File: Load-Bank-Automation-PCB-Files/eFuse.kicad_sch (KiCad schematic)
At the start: 14 parts, among them Q3 NMOS, U7 LM5069MM-1

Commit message: Nothing new
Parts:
- R13: value R -> 6.5m
- R18: value 100k -> R_{PGD}
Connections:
- net V_{DD} is gone; now on net V+_{in}: R18.2
- net PGOOD: no longer names the net of R18.1, U7.8 (PGD)
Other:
- note added: "Calculations: * Current Limit: Is when 48.5mv<=V_{CL}<=61.5mv -> 48.5mV/7.5A=R_{13}=${/c82c4769-33eb-46b7-8d07-39045014a3da/eb9b9647-818b-4f6a-aec9-7481a1a3b43c/4e0619fb-b7ea-493d-b159-72357478fd6a/6879bab9-d947-4c13-8fcf-4238d3b2053c:value}ohm * R_{PWR} is used to determine the thermal limit of Q1 MOSFET, the chip uses the current from R_{sense} and the voltage from SENSE and OUT pins to find th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"
- moved on the sheet: C32, C33, C34, D2, D4, Q3, R13, R14, R15, R16, R17, R18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

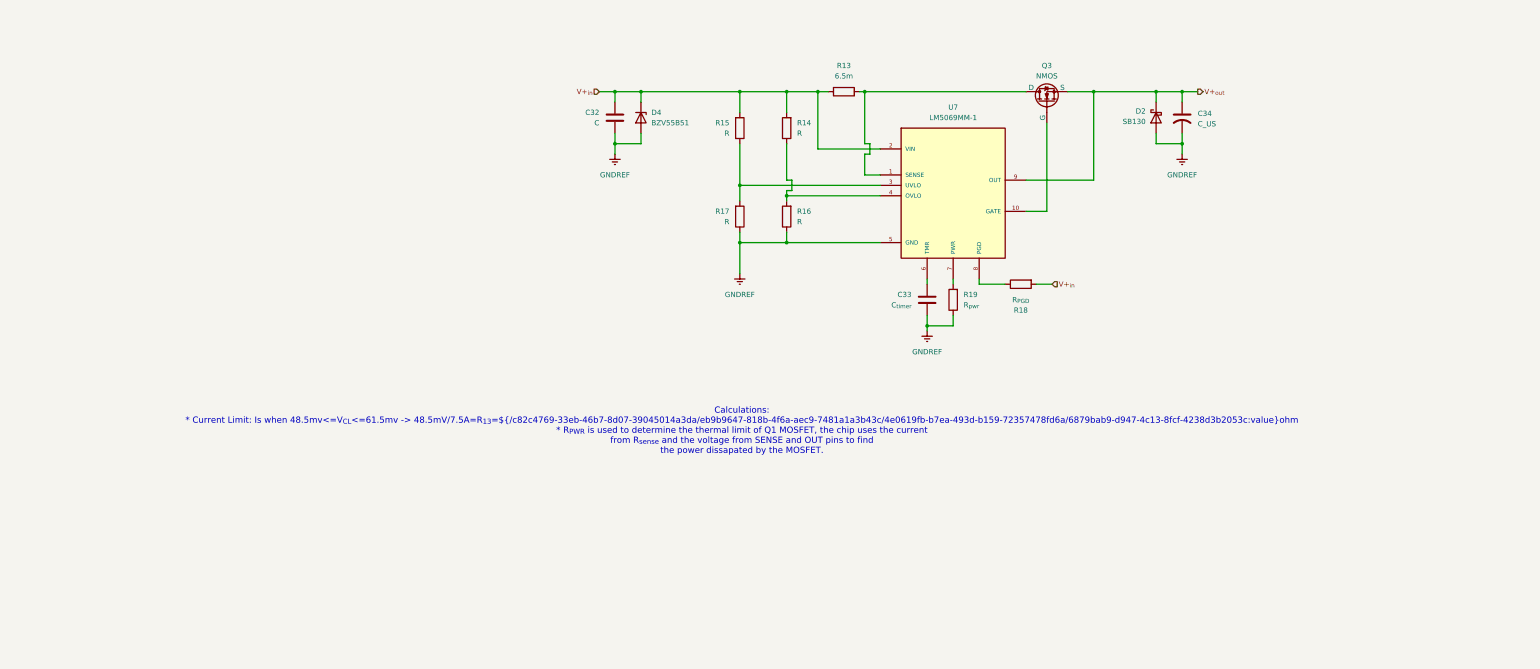
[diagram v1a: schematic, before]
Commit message: Completed eFuse and Starting on Layout
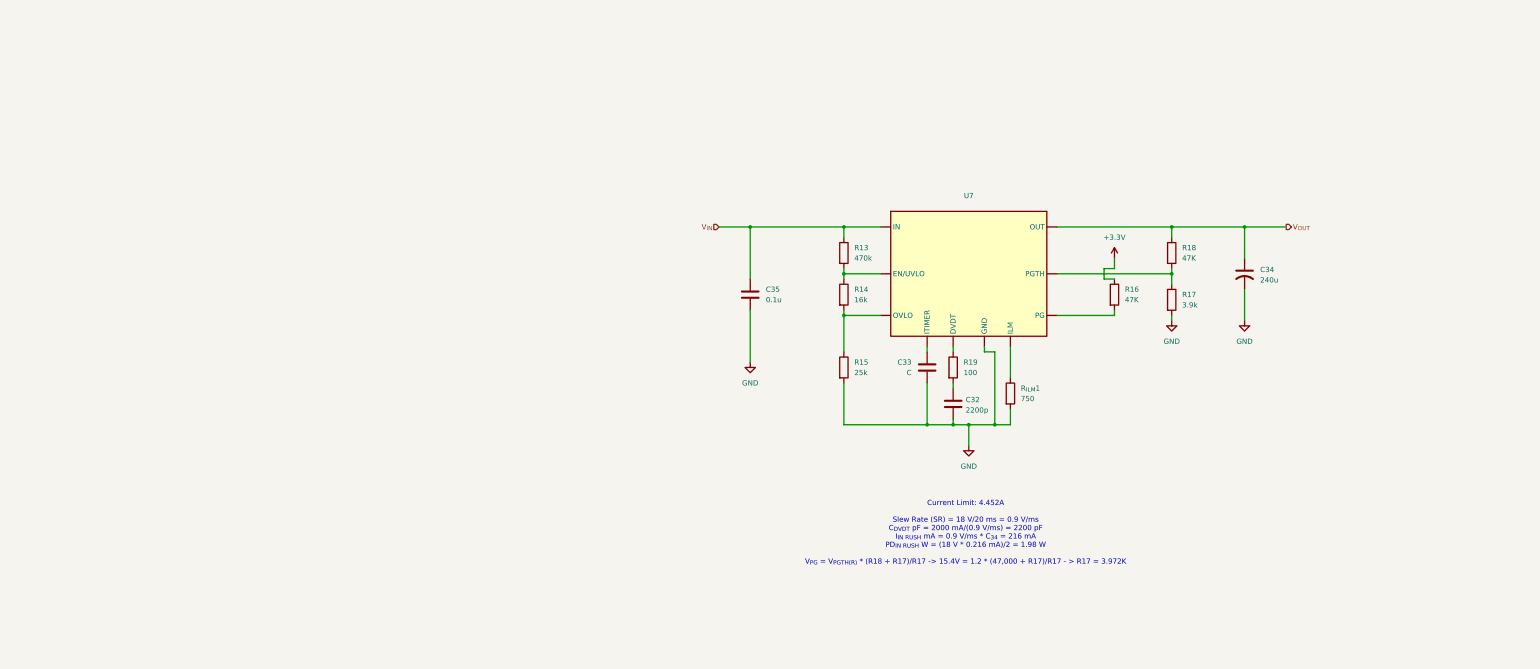
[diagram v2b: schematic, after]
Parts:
- removed D2: SB130, Diode_THT:D_DO-41_SOD81_P10.16mm_Horizontal, symbol Diode:SB130
- removed D4: BZV55B51, Diode_SMD:D_MiniMELF, symbol Diode:BZV55B51
- removed Q3: NMOS, symbol Simulation_SPICE:NMOS
- removed U7: LM5069MM-1, LM5069MM-1:SOP50P490X110-10N, symbol LM5069MM-1:LM5069MM-1
- added C35: 0.1u, Resistor_SMD:R_0603_1608Metric, symbol Device:C
- added R_{ILM}1: 750, Resistor_SMD:R_0603_1608Metric, symbol Device:R
- added U7: ~, symbol Power_Protection:TPS259474LRPWR
- C32: value C -> 2200p; footprint (none) -> Resistor_SMD:R_0603_1608Metric
- C33: value C_{timer} -> C; footprint (none) -> Resistor_SMD:R_0603_1608Metric
- C34: value C_US -> 240u; footprint (none) -> Resistor_SMD:R_0603_1608Metric
- R13: value 6.5m -> 470k; footprint (none) -> Resistor_SMD:R_0603_1608Metric
- R14: value R -> 16k; footprint (none) -> Resistor_SMD:R_0603_1608Metric
- R15: value R -> 25k; footprint (none) -> Resistor_SMD:R_0603_1608Metric
- R16: value R -> 47K; footprint (none) -> Resistor_SMD:R_0603_1608Metric
- R17: value R -> 3.9k; footprint (none) -> Resistor_SMD:R_0603_1608Metric
- R18: value R_{PGD} -> 47K; footprint (none) -> Resistor_SMD:R_0603_1608Metric
- R19: value R_{pwr} -> 100; footprint (none) -> Resistor_SMD:R_0603_1608Metric
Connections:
- net V+_{out} is gone; now on net V_{OUT}: C34.1
- net GND: now reaches C33.1
- net GND: now also C32.2, C34.2, R15.2, R17.2, C35.2, R_{ILM}1.2, U7. (PG)
- net at R16.2: now also U7. (PG); no longer R14.1
- net at R15.1: now also R14.2, U7. (PG); no longer R17.2
- net V_{IN}: now reaches R13.1
- net V_{IN}: now also C35.1, U7. (PG)
- net at R19.2: now also C32.1
- net V_{OUT}: now reaches R18.1
- net V_{OUT}: now also U7. (PG)
- removed net GNDREF: C32.2, C33.2, C34.2, R16.1, R17.1, R19.1
- removed net V+_{in}: C32.1, R13.2, R14.2, R15.2, R18.2
- new net: R19.1, U7. (PG)
- new net: R_{ILM}1.1, U7. (PG)
- new net: R13.2, R14.1, U7. (PG)
- new net: R17.1, R18.2, U7. (PG)
- new net: C33.2, U7. (PG)
- new net +3.3V: R16.1
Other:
- note added: "Current Limit: 4.452A Slew Rate (SR) = 18 V/20 ms = 0.9 V/ms C_{DVDT} pF = 2000 mA/(0.9 V/ms) = 2200 pF I_{IN RUSH} mA = 0.9 V/ms * C_{34} = 216 mA PD_{IN RUSH} W = (18 V * 0.216 mA)/2 = 1.98 W V_{PG} = V_{PGTH(R)} * (R18 + R17)/R17 -> 15.4V = 1.2 * (47,000 + R17)/R17 - > R17 = 3.972K"
- note removed: "Calculations: * Current Limit: Is when 48.5mv<=V_{CL}<=61.5mv -> 48.5mV/7.5A=R_{13}=${/c82c4769-33eb-46b7-8d07-39045014a3da/eb9b9647-818b-4f6a-aec9-7481a1a3b43c/4e0619fb-b7ea-493d-b159-72357478fd6a/6879bab9-d947-4c13-8fcf-4238d3b2053c:value}ohm * R_{PWR} is used to determine the thermal limit of Q1 MOSFET, the chip uses the current from R_{sense} and the voltage from SENSE and OUT pins to find th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"

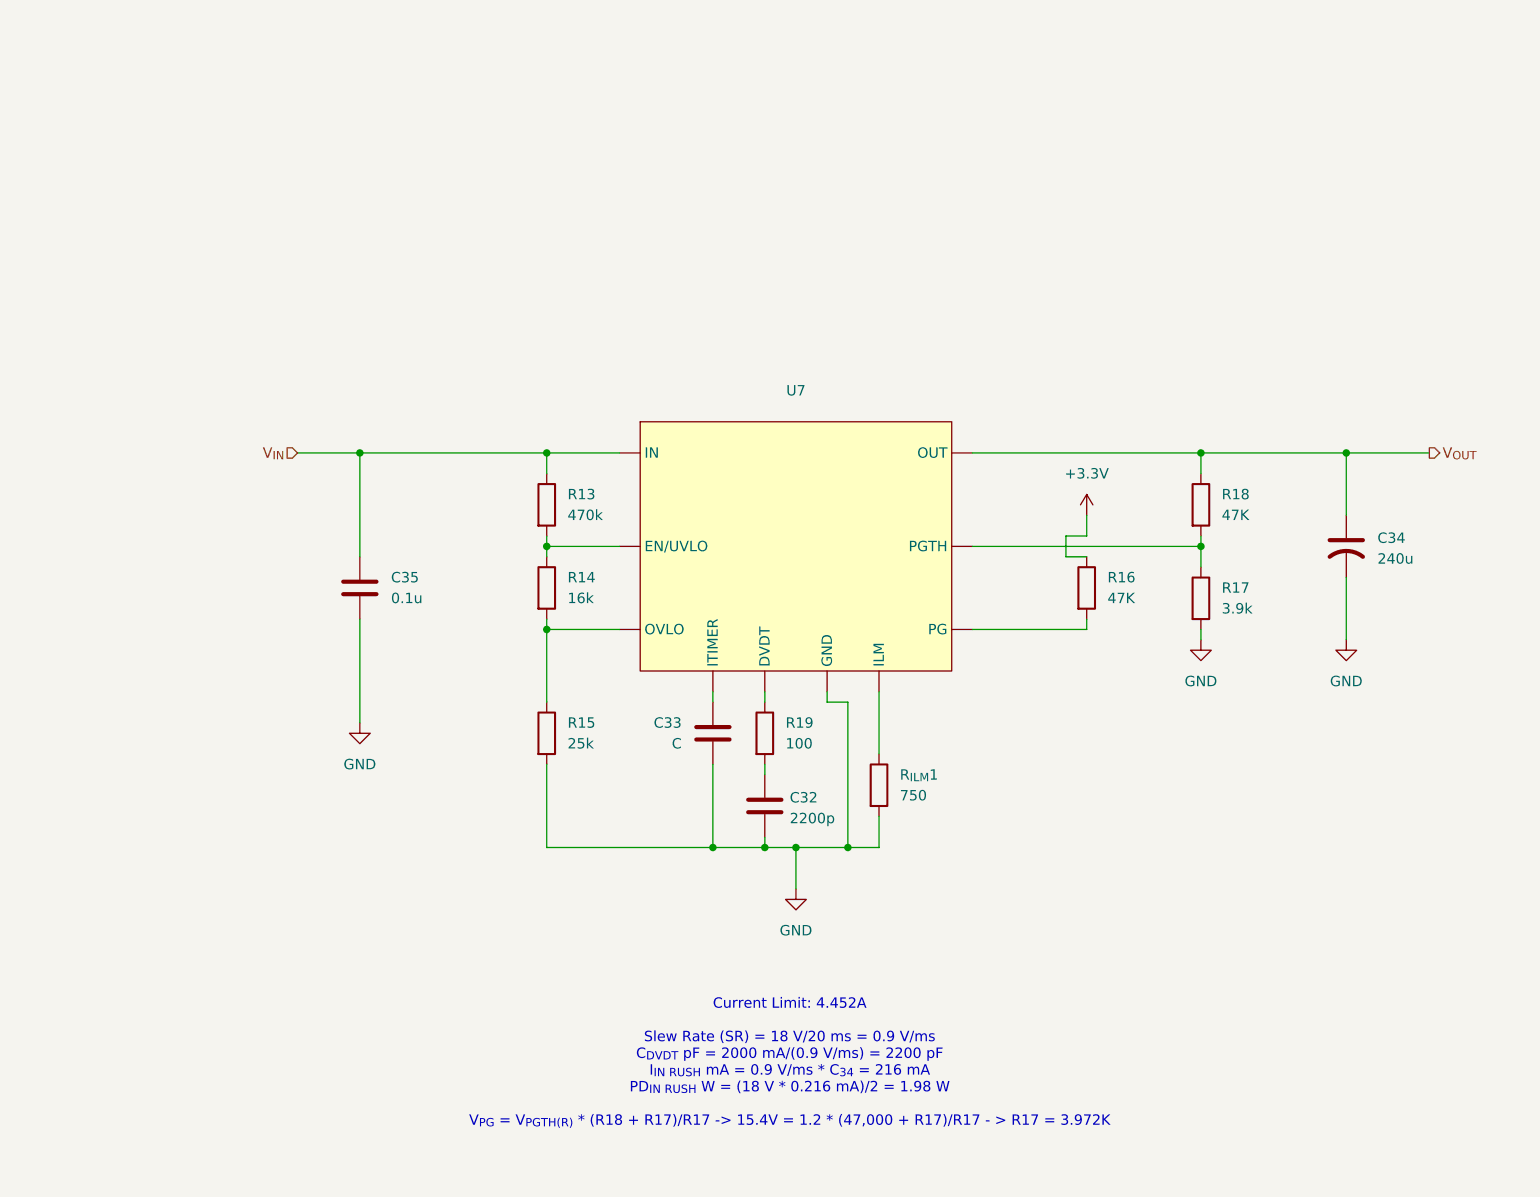
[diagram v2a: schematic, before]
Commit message: New MCU, Configured Pins, Attached some footprints
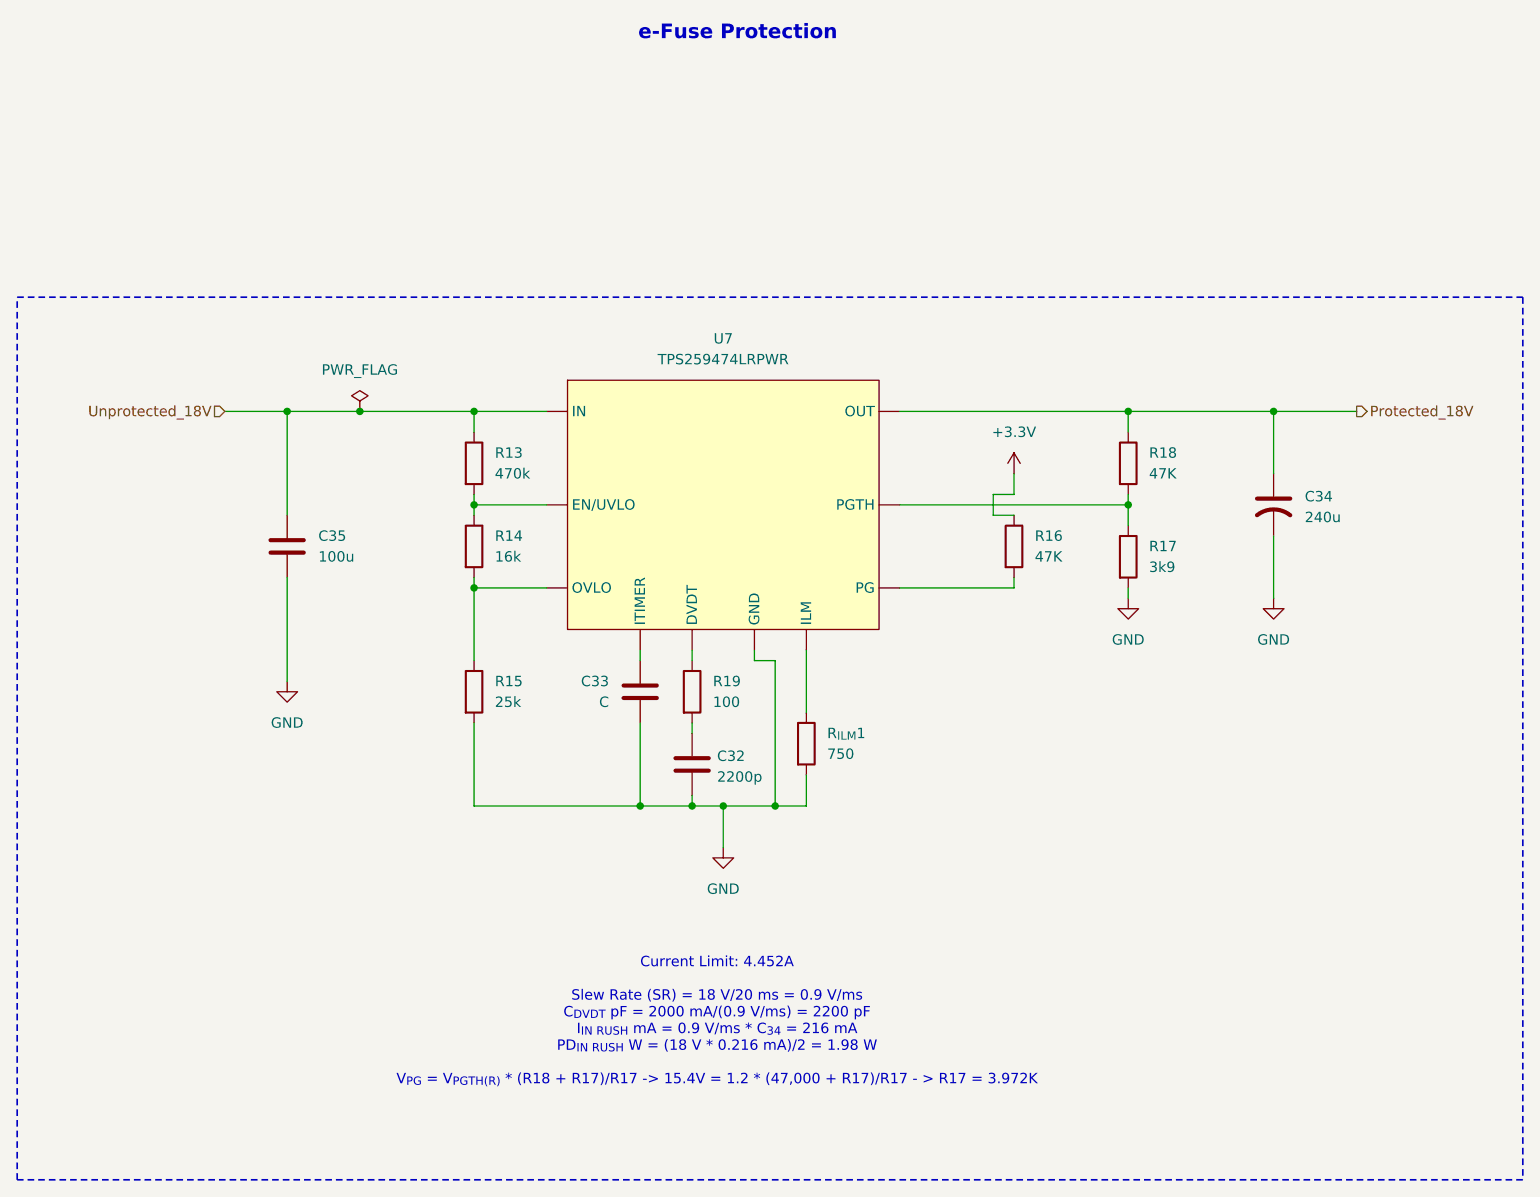
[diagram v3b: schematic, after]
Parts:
- C35: value 0.1u -> 100u
- R17: value 3.9k -> 3k9
- U7: value ~ -> TPS259474LRPWR; footprint (none) -> eFuse_TPS259474LRPWR:RPW0010A-MFG
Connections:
- net V_{IN} renamed Unprotected_18V
- net V_{OUT} renamed Protected_18V
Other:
- note added: "e-Fuse Protection"
- moved on the sheet: C32, C33, C34, C35, R13, R14, R15, R16, R17, R18, R19, R_{ILM}1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

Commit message: Schematic revision for review
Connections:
- net GND: now also U7.8 (GND); no longer U7. (PG)
- net Protected_18V: now also U7.6 (OUT); no longer U7. (PG)
- net Unprotected_18V: now also U7.5 (IN); no longer U7. (PG)
- net at R16.2: now also U7.3 (PG); no longer U7. (PG)
- net at R19.1: now also U7.7 (DVDT); no longer U7. (PG)
- net at R_{ILM}1.1: now also U7.9 (ILM); no longer U7. (PG)
- net at R13.2, R14.1: now also U7.1 (EN/UVLO); no longer U7. (PG)
- net at R17.1, R18.2: now also U7.4 (PGTH); no longer U7. (PG)
- net at R14.2, R15.1: now also U7.2 (OVLO); no longer U7. (PG)
- net at C33.2: now also U7.10 (ITIMER); no longer U7. (PG)
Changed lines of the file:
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@@
+	)
+	(junction
+		(at 185.42 72.39)
+		(diameter 0)
+		(color 0 0 0 0)
 	)
 	(junction
@@
 	(wire
 		(pts
+			(xy 175.26 71.12) (xy 175.26 72.39)
+		)
+		(stroke
+			(width 0)
+			(type default)
+		)
+	)
+	(wire
+		(pts
 			(xy 182.88 76.2) (xy 182.88 73.66)
 		)
@@
 	(wire
 		(pts
+			(xy 185.42 72.39) (xy 185.42 71.12)
+		)
+		(stroke
+			(width 0)
+			(type default)
+		)
+	)
+	(wire
+		(pts
 			(xy 199.39 63.5) (xy 199.39 66.04)
 		)
@@
 	(wire
 		(pts
+			(xy 175.26 72.39) (xy 185.42 72.39)
+		)
+		(stroke
+			(width 0)
+			(type default)
+		)
+	)
+	(wire
+		(pts
 			(xy 182.88 73.66) (xy 185.42 73.66)
 		)
@@
 	(wire
 		(pts
-			(xy 185.42 73.66) (xy 185.42 71.12)
+			(xy 185.42 73.66) (xy 185.42 72.39)
 		)
 		(stroke
@@
 	)
 	(symbol
-		(lib_id "Power_Protection:TPS259474LRPWR")
-		(at 149.86 74.93 0)
-		(unit 1)
-		(exclude_from_sim no)
-		(in_bom yes)
-		(on_board yes)
-		(dnp no)
-		(fields_autoplaced yes)
-		(property "Reference" "U7"
-			(at 149.86 54.61 0)
-			(effects
-				(font
-					(size 1.27 1.27)
-				)
-			)
-		)
-		(property "Value" "TPS259474LRPWR"
-			(at 149.86 57.15 0)
-			(effects
-				(font
-					(size 1.27 1.27)
-				)
-			)
-		)
-		(property "Footprint" "eFuse_TPS259474LRPWR:RPW0010A-MFG"
-			(at 149.86 74.93 0)
-			(effects
-				(font
-					(size 1.27 1.27)
-				)
-				(hide yes)
-			)
-		)
-		(property "Datasheet" "https://www.ti.com/lit/ds/symlink/tps25947.pdf?HQS=dis-dk-null-digikeymode-dsf-pf-null-wwe&ts=1758509314473"
-			(at 149.86 74.93 0)
-			(effects
-				(font
-					(size 1.27 1.27)
-				)
-				(hide yes)
-			)
-		)
-		(property "Description" ""
-			(at 149.86 74.93 0)
-			(effects
-				(font
-					(size 1.27 1.27)
-				)
-				(hide yes)
-			)
-		)
-		(pin ""
-		)
-		(pin ""
-		)
-		(pin ""
-		)
-		(pin ""
-		)
-		(pin ""
-		)
-		(pin ""
-		)
-		(pin ""
-		)
-		(pin ""
-		)
-		(pin ""
-		)
-		(pin ""
-		)
-		(instances
-			(project ""
-				(path "/c82c4769-33eb-46b7-8d07-39045014a3da/eb9b9647-818b-4f6a-aec9-7481a1a3b43c/4e0619fb-b7ea-493d-b159-72357478fd6a"
-					(reference "U7")
-					(unit 1)
-				)
-			)
-		)
-	)
-	(symbol
 		(lib_id "Device:R")
 		(at 199.39 81.28 0)
@@
 	)
 	(symbol
+		(lib_id "power:PWR_FLAG")
+		(at 175.26 71.12 0)
+		(unit 1)
+		(exclude_from_sim no)
+		(in_bom yes)
+		(on_board yes)
+		(dnp no)
+		(fields_autoplaced yes)
+		(property "Reference" "#FLG05"
+			(at 175.26 69.215 0)
+			(effects
+				(font
+					(size 1.27 1.27)
+				)
+				(hide yes)
+			)
+		)
+		(property "Value" "PWR_FLAG"
+			(at 175.26 66.04 0)
+			(effects
+				(font
+					(size 1.27 1.27)
+				)
+			)
+		)
+		(property "Footprint" ""
+			(at 175.26 71.12 0)
+			(effects
+				(font
+					(size 1.27 1.27)
+				)
+				(hide yes)
+			)
+		)
+		(property "Datasheet" "~"
+			(at 175.26 71.12 0)
+			(effects
+				(font
+					(size 1.27 1.27)
+				)
+				(hide yes)
+			)
+		)
+		(property "Description" "Special symbol for telling ERC where power comes from"
+			(at 175.26 71.12 0)
+			(effects
+				(font
+					(size 1.27 1.27)
+				)
+				(hide yes)
+			)
+		)
+		(pin "1"
+		)
+		(instances
+			(project "Main Board"
+				(path "/c82c4769-33eb-46b7-8d07-39045014a3da/eb9b9647-818b-4f6a-aec9-7481a1a3b43c/4e0619fb-b7ea-493d-b159-72357478fd6a"
+					(reference "#FLG05")
+					(unit 1)
+				)
+			)
+		)
+	)
+	(symbol
 		(lib_id "power:GND")
 		(at 199.39 86.36 0)
@@
 					(unit 1)
 				)
+			)
+		)
+	)
+	(symbol
+		(lib_name "TPS259474LRPWR_1")
+		(lib_id "Power_Protection:TPS259474LRPWR")
+		(at 149.86 74.93 0)
+		(unit 1)
+		(exclude_from_sim no)
+		(in_bom yes)
+		(on_board yes)
+		(dnp no)
+		(fields_autoplaced yes)
+		(property "Reference" "U7"
+			(at 149.86 55.88 0)
+			(effects
+				(font
+					(size 1.27 1.27)
+				)
+			)
+		)
+		(property "Value" "TPS259474LRPWR"
+			(at 149.86 58.42 0)
+			(effects
+				(font
+					(size 1.27 1.27)
+				)
+			)
+		)
+		(property "Footprint" "eFuse_TPS259474LRPWR:RPW0010A-MFG"
+			(at 149.86 74.93 0)
+			(effects
+				(font
+					(size 1.27 1.27)
+				)
+				(hide yes)
+			)
+		)
+		(property "Datasheet" "https://www.ti.com/lit/ds/symlink/tps25947.pdf?HQS=dis-dk-null-digikeymode-dsf-pf-null-wwe&ts=1758509314473"
+			(at 149.86 74.93 0)
+			(effects
+				(font
+					(size 1.27 1.27)
+				)
+				(hide yes)
+			)
+		)
+		(property "Description" ""
+			(at 149.86 74.93 0)
+			(effects
+				(font
+					(size 1.27 1.27)
+				)
+				(hide yes)
+			)
+		)
+		(pin "5"
+		)
+		(pin "2"
+		)
+		(pin "7"
+		)
+		(pin "9"
+		)
+		(pin "4"
+		)
+		(pin "8"
+		)
+		(pin "6"
+		)
+		(pin "1"
+		)
+		(pin "3"
+		)
+		(pin "10"
+		)
+		(instances
+			(project ""
+				(path "/c82c4769-33eb-46b7-8d07-39045014a3da/eb9b9647-818b-4f6a-aec9-7481a1a3b43c/4e0619fb-b7ea-493d-b159-72357478fd6a"
+					(reference "U7")
+					(unit 1)
+				)
